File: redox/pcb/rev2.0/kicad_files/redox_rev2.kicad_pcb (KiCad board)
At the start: 2 copper layers, 162.2 x 138.8 mm, 150 parts, among them J1 AVR-ISP-6, J2 OLED-SSD1306, K1 KEYSW, K10 KEYSW, K11 KEYSW, K12 KEYSW, K13 KEYSW, K14 KEYSW, K15 KEYSW, K16 KEYSW, K17 KEYSW, K18 KEYSW, K19 KEYSW, K2 KEYSW, K20 KEYSW, K21 KEYSW, K22 KEYSW, K23 KEYSW, K24 KEYSW, K25 KEYSW, K26 KEYSW, K27 KEYSW, K28 KEYSW, K29 KEYSW, K3 KEYSW, K30 KEYSW, K31 KEYSW, K32 KEYSW, K33 KEYSW, K34 KEYSW, K35 KEYSW, K4 KEYSW, K5 KEYSW, K6 KEYSW, K7 KEYSW, K8 KEYSW, K9 KEYSW, Q1 2N7002, U1 PRTR5V0U2X, U2 ATmega32U4, Y1 16Mhz

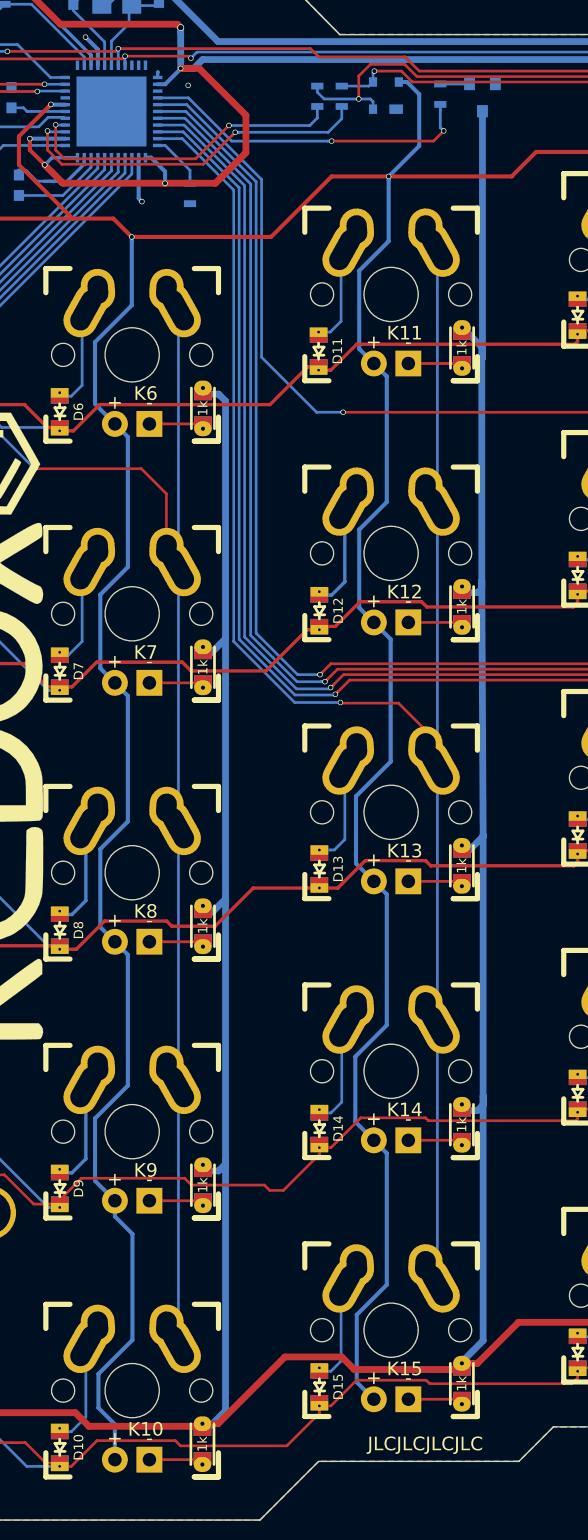
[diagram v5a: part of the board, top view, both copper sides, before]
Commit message: try to add themal viad for the ATMEGA32u4-MU
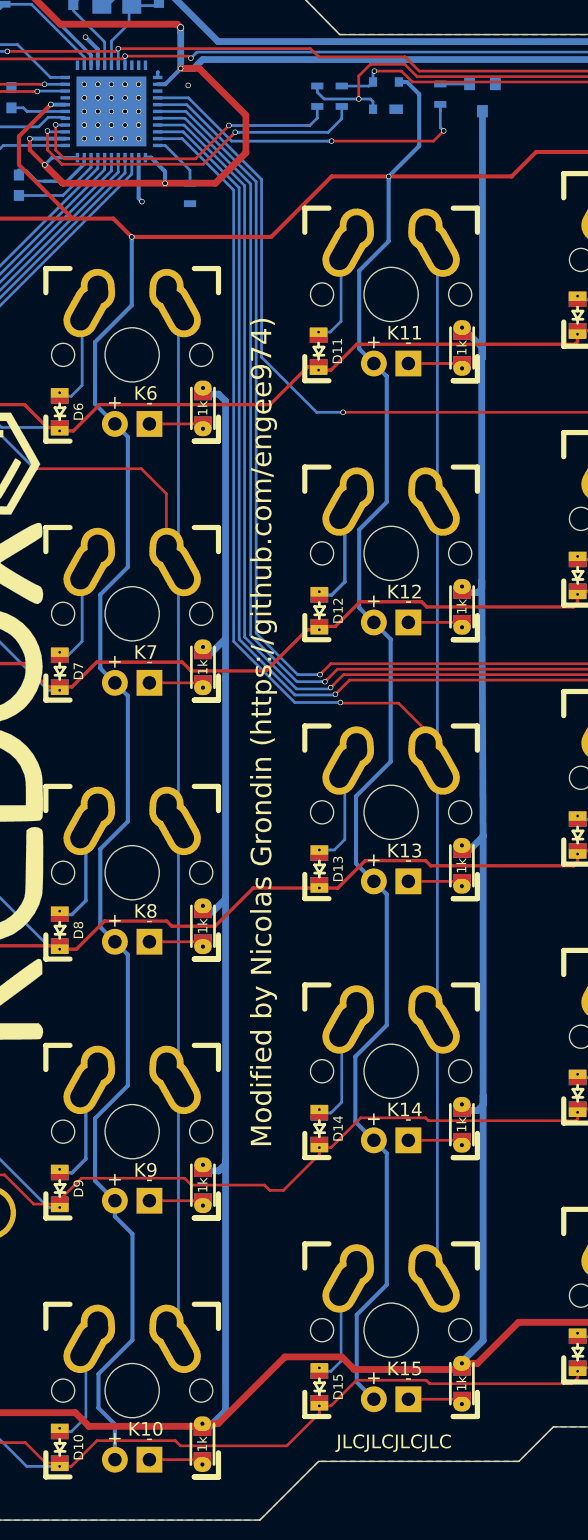
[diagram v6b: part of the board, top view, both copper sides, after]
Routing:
- net (no net): vias 0 -> 25
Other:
- board text added: "Modified by Nicolas Grondin (https://github.com/engee974)"
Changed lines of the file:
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@@
   (general
     (thickness 1.6)
-    (drawings 38)
-    (tracks 1439)
+    (drawings 40)
+    (tracks 1464)
     (zones 0)
     (modules 150)
@@
     (0 F.Cu signal)
     (31 B.Cu signal)
-    (32 B.Adhes user)
-    (33 F.Adhes user)
-    (34 B.Paste user)
-    (35 F.Paste user)
+    (32 B.Adhes user hide)
+    (33 F.Adhes user hide)
+    (34 B.Paste user hide)
+    (35 F.Paste user hide)
     (36 B.SilkS user)
     (37 F.SilkS user)
-    (38 B.Mask user)
-    (39 F.Mask user)
-    (40 Dwgs.User user)
+    (38 B.Mask user hide)
+    (39 F.Mask user hide)
+    (40 Dwgs.User user hide)
     (41 Cmts.User user)
     (42 Eco1.User user)
@@
     (tags SOT-23)
     (attr smd)
-    (fp_text reference Q1 (at 0 2.5 90) (layer B.SilkS)
+    (fp_text reference Q1 (at 2.35 0 180) (layer B.SilkS)
       (effects (font (size 1 1) (thickness 0.15)) (justify mirror))
     )
@@
     )
   )
-  (gr_text JLCJLCJLCJLC (at 134.6 146.8) (layer F.SilkS)
+  (gr_text "Modified by Nicolas Grondin (https://github.com/engee974)" (at 122.565 94.688 90) (layer B.SilkS)
+    (effects (font (size 1.5 1.5) (thickness 0.3)) (justify mirror))
+  )
+  (gr_text "Modified by Nicolas Grondin (https://github.com/engee974)" (at 122.565 94.434 90) (layer F.SilkS)
+    (effects (font (size 1.5 1.5) (thickness 0.3)))
+  )
+  (gr_text JLCJLCJLCJLC (at 132.3 146.65) (layer F.SilkS)
     (effects (font (size 1 1) (thickness 0.15)))
   )
@@
   (gr_line (start 79.502 133.35) (end 84.328 138.176) (angle 90) (layer Edge.Cuts) (width 0.1))
   (gr_line (start 79.5 57.2) (end 79.502 133.35) (angle 90) (layer Edge.Cuts) (width 0.1))
+  (via (at 109.506 48.768) (size 0.4) (drill 0.3) (layers F.Cu B.Cu) (net 0))
+  (via (at 110.506 48.768) (size 0.4) (drill 0.3) (layers F.Cu B.Cu) (net 0))
+  (via (at 111.506 48.768) (size 0.4) (drill 0.3) (layers F.Cu B.Cu) (net 0))
+  (via (at 112.506 48.768) (size 0.4) (drill 0.3) (layers F.Cu B.Cu) (net 0))
+  (via (at 113.506 48.768) (size 0.4) (drill 0.3) (layers F.Cu B.Cu) (net 0))
+  (via (at 109.506 49.768) (size 0.4) (drill 0.3) (layers F.Cu B.Cu) (net 0))
+  (via (at 112.506 49.768) (size 0.4) (drill 0.3) (layers F.Cu B.Cu) (net 0))
+  (via (at 113.506 49.768) (size 0.4) (drill 0.3) (layers F.Cu B.Cu) (net 0))
+  (via (at 111.506 49.768) (size 0.4) (drill 0.3) (layers F.Cu B.Cu) (net 0))
+  (via (at 110.506 49.768) (size 0.4) (drill 0.3) (layers F.Cu B.Cu) (net 0))
+  (via (at 109.506 46.768) (size 0.4) (drill 0.3) (layers F.Cu B.Cu) (net 0))
+  (via (at 112.506 46.768) (size 0.4) (drill 0.3) (layers F.Cu B.Cu) (net 0))
+  (via (at 113.506 46.768) (size 0.4) (drill 0.3) (layers F.Cu B.Cu) (net 0))
+  (via (at 112.506 47.768) (size 0.4) (drill 0.3) (layers F.Cu B.Cu) (net 0))
+  (via (at 113.506 47.768) (size 0.4) (drill 0.3) (layers F.Cu B.Cu) (net 0))
+  (via (at 110.506 47.768) (size 0.4) (drill 0.3) (layers F.Cu B.Cu) (net 0))
+  (via (at 109.506 47.768) (size 0.4) (drill 0.3) (layers F.Cu B.Cu) (net 0))
+  (via (at 111.506 47.768) (size 0.4) (drill 0.3) (layers F.Cu B.Cu) (net 0))
+  (via (at 111.506 46.768) (size 0.4) (drill 0.3) (layers F.Cu B.Cu) (net 0))
+  (via (at 110.506 46.768) (size 0.4) (drill 0.3) (layers F.Cu B.Cu) (net 0))
+  (via (at 112.506 50.768) (size 0.4) (drill 0.3) (layers F.Cu B.Cu) (net 0))
+  (via (at 113.506 50.768) (size 0.4) (drill 0.3) (layers F.Cu B.Cu) (net 0))
+  (via (at 110.506 50.768) (size 0.4) (drill 0.3) (layers F.Cu B.Cu) (net 0))
+  (via (at 109.506 50.768) (size 0.4) (drill 0.3) (layers F.Cu B.Cu) (net 0))
+  (via (at 111.506 50.768) (size 0.4) (drill 0.3) (layers F.Cu B.Cu) (net 0))
   (segment (start 106.796 72.016) (end 107.696 72.016) (width 0.25) (layer F.Cu) (net 1))
   (segment (start 87.434999 70.337001) (end 105.117001 70.337001) (width 0.25) (layer F.Cu) (net 1))

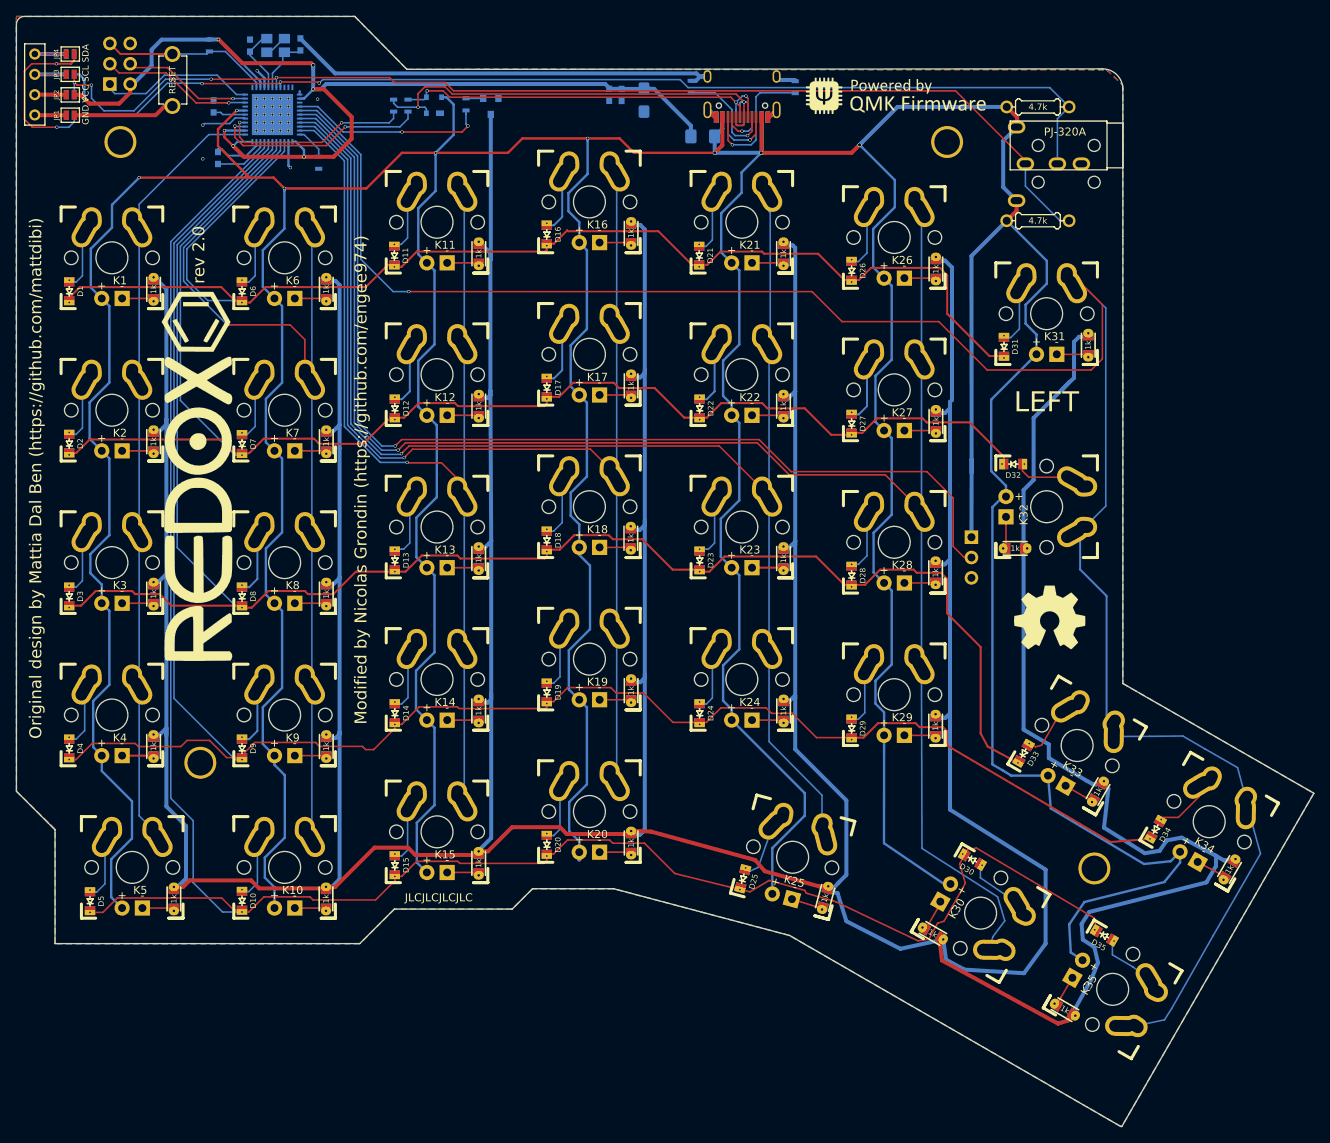
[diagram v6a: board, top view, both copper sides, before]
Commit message: Change ATùega32u4-MU QFN-44 footprint from standard library
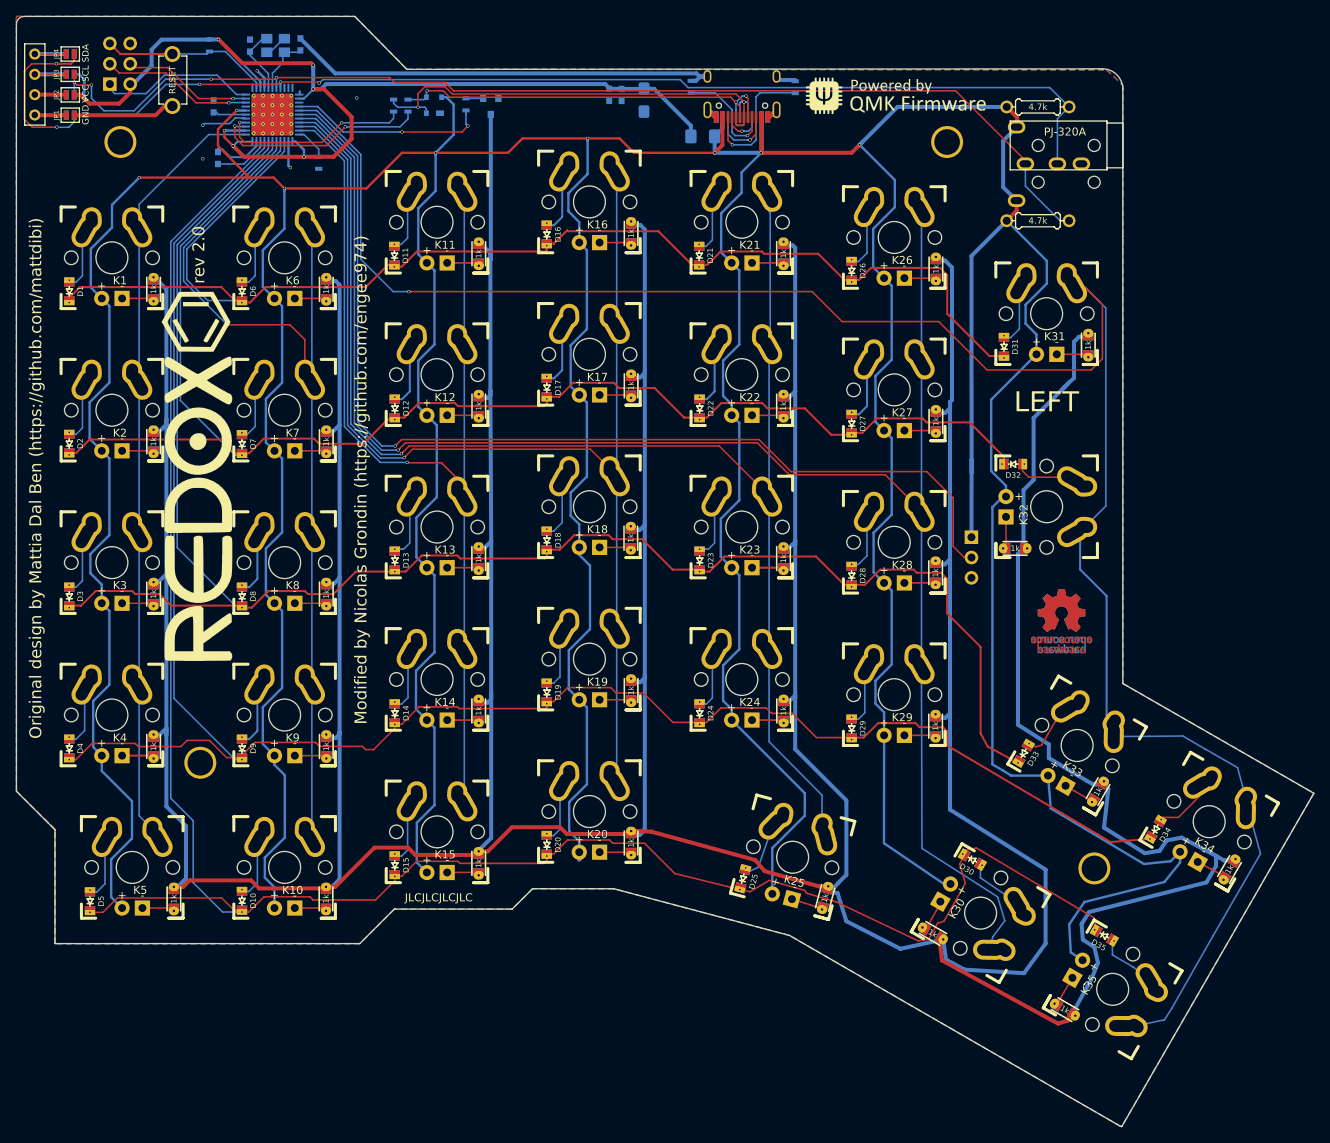
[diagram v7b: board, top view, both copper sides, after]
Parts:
- removed REF*** (x2): OSHW-Logo2_14.6x12mm_SilkScreen, redox_footprints:OSHW-Symbol_8.9x8mm_SilkScreen
- added REF**: OSHW-Logo_7.5x8mm_Copper, Symbol:OSHW-Logo_7.5x8mm_Copper, B.Cu at (210.2, 112.1)
- added REF**: OSHW-Logo_7.5x8mm_Copper, Symbol:OSHW-Logo_7.5x8mm_Copper, F.Cu at (210.2, 112.1)
- U2: footprint Keebio-Parts:QFN-44-1EP_7x7mm_Pitch0.5mm -> Package_DFN_QFN:QFN-44-1EP_7x7mm_P0.5mm_EP5.2x5.2mm_ThermalVias
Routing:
- net LEDGND: track 825.6 -> 826.2 mm
- net (no net): vias 25 -> 0

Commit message: PCB - Add OSHW copper logo
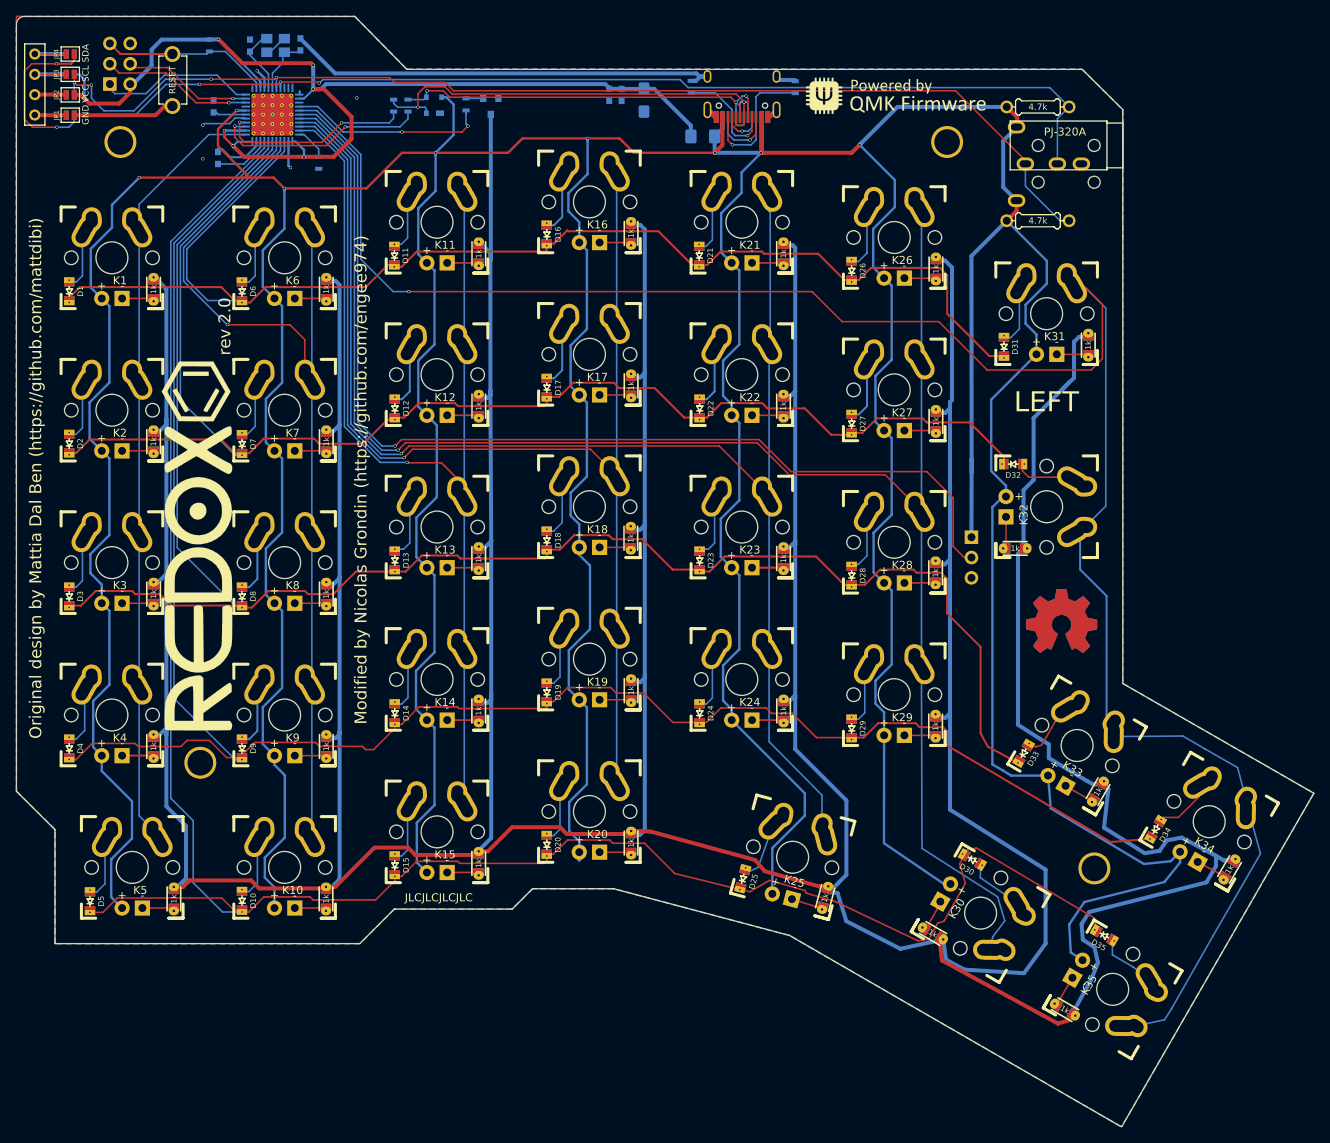
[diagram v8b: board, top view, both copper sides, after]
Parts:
- REF** (x2): value OSHW-Logo_7.5x8mm_Copper -> OSHW-Symbol_8.9x8mm_Copper; footprint Symbol:OSHW-Logo_7.5x8mm_Copper -> redox_footprints:OSHW-Symbol_8.9x8mm_Copper
- moved REDOX_BOTTOM 8.70 mm to (102.2, 102.7)
- moved REDOX_FRONT 8.70 mm to (102.2, 102.7)
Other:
- outline, holes or cut-outs redrawn
